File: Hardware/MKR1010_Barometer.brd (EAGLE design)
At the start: 160 x 100 mm, 2 parts

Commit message: schematic capture
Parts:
- added D1: 1N4001, SparkFun-DiscreteSemi:DIODE-1N4001
- added J1: (no value), con-jack:SPC4077
- added J2, J3: 1X2-3.5MM, adafruit:1X2-3.5MM
- added M1: MOTOR10MM, SparkFun-Electromechanical:VIBE-MOTOR-10MM
- added T1: TIP122, transistor:TO220
- R1: value (none) -> 220
- renumbered U$1 to MKR1010
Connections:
- new net GND: D1.A, J1.1, J3.1, T1.3
- new net N$2: R1.1, T1.1
- new net N$3: D1.C, M1.-, T1.2
- new net N$4: J1.3, J2.2, M1.+, MKR1010.P$23
- new net N$5: J2.1, MKR1010.P$7
- net N$1: now also MKR1010.P$6; no longer MKR1010.P$25
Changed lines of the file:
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@@
 <?xml version="1.0" encoding="utf-8"?>
 <!DOCTYPE eagle SYSTEM "eagle.dtd">
-<eagle version="9.2.1">
+<eagle version="9.2.2">
 <drawing>
 <settings>
@@
 <layer number="112" name="tSilk" color="7" fill="1" visible="no" active="yes"/>
 <layer number="113" name="ReferenceLS" color="7" fill="1" visible="no" active="no"/>
+<layer number="114" name="Badge_Outline" color="7" fill="1" visible="yes" active="yes"/>
+<layer number="115" name="ReferenceISLANDS" color="7" fill="1" visible="yes" active="yes"/>
 <layer number="116" name="Patch_BOT" color="9" fill="4" visible="no" active="yes"/>
 <layer number="118" name="Rect_Pads" color="7" fill="1" visible="no" active="no"/>
@@
 </autorouter>
 <elements>
-<element name="U$1" library="adafruit" library_urn="urn:adsk.eagle:library:420" package="ARDUINOMICRO" value="ARDUINOMICRO" x="34.29" y="73.66" smashed="yes"/>
-<element name="R1" library="adafruit" library_urn="urn:adsk.eagle:library:420" package="0207/12" value="" x="36.83" y="53.34" smashed="yes" rot="R90">
+<element name="MKR1010" library="adafruit" library_urn="urn:adsk.eagle:library:420" package="ARDUINOMICRO" value="ARDUINOMICRO" x="34.29" y="73.66" smashed="yes"/>
+<element name="R1" library="adafruit" library_urn="urn:adsk.eagle:library:420" package="0207/12" value="220" x="36.83" y="53.34" smashed="yes" rot="R90">
 <attribute name="NAME" x="35.433" y="50.165" size="1.27" layer="25" ratio="10" rot="R90"/>
 <attribute name="VALUE" x="37.5158" y="51.054" size="1.27" layer="27" ratio="10" rot="R90"/>
+</element>
+<element name="D1" library="SparkFun-DiscreteSemi" library_urn="urn:adsk.eagle:library:514" package="DIODE-1N4001" package3d_urn="urn:adsk.eagle:package:38453/1" value="1N4001" x="6.35" y="-2.54" smashed="yes">
+<attribute name="NAME" x="6.35" y="-1.016" size="0.6096" layer="25" font="vector" ratio="20" align="bottom-center"/>
+<attribute name="PROD_ID" value="DIO-09176" x="6.35" y="-2.54" size="1.778" layer="27" display="off"/>
+<attribute name="VALUE" x="6.35" y="-4.064" size="0.6096" layer="27" font="vector" ratio="20" align="top-center"/>
+</element>
+<element name="T1" library="transistor" library_urn="urn:adsk.eagle:library:402" package="TO220" package3d_urn="urn:adsk.eagle:package:29897/1" value="TIP122" x="-6.35" y="3.81" smashed="yes">
+<attribute name="NAME" x="-10.16" y="9.017" size="1.778" layer="25" ratio="10"/>
+<attribute name="VALUE" x="-10.287" y="6.35" size="1.778" layer="27" ratio="10"/>
+</element>
+<element name="M1" library="SparkFun-Electromechanical" library_urn="urn:adsk.eagle:library:516" package="VIBE-MOTOR-10MM" package3d_urn="urn:adsk.eagle:package:38555/1" value="MOTOR10MM" x="-2.54" y="-10.16" smashed="yes">
+<attribute name="NAME" x="-7.747" y="-10.16" size="0.6096" layer="25" font="vector" ratio="20" rot="R90" align="bottom-center"/>
+<attribute name="PROD_ID" value="COMP-08572" x="-2.54" y="-10.16" size="1.778" layer="27" display="off"/>
+<attribute name="SF_SKU" value="ROB-08449" x="-2.54" y="-10.16" size="1.778" layer="27" display="off"/>
+<attribute name="VALUE" x="-7.239" y="-10.16" size="0.6096" layer="27" font="vector" ratio="20" rot="R90" align="top-center"/>
+</element>
+<element name="J1" library="con-jack" library_urn="urn:adsk.eagle:library:154" package="SPC4077" package3d_urn="urn:adsk.eagle:package:7492/1" value="" x="0" y="-25.4" smashed="yes">
+<attribute name="MF" value="" x="0" y="-25.4" size="1.778" layer="27" display="off"/>
+<attribute name="MPN" value="" x="0" y="-25.4" size="1.778" layer="27" display="off"/>
+<attribute name="NAME" x="-10.16" y="-20.32" size="1.27" layer="25"/>
+<attribute name="OC_FARNELL" value="unknown" x="0" y="-25.4" size="1.778" layer="27" display="off"/>
+<attribute name="OC_NEWARK" value="unknown" x="0" y="-25.4" size="1.778" layer="27" display="off"/>
+<attribute name="VALUE" x="-10.16" y="-31.75" size="1.27" layer="27"/>
+</element>
+<element name="J2" library="adafruit" library_urn="urn:adsk.eagle:library:420" package="1X2-3.5MM" package3d_urn="urn:adsk.eagle:package:6240635/1" value="1X2-3.5MM" x="-16.51" y="-26.67" smashed="yes">
+<attribute name="NAME" x="-13.51" y="-21.67" size="1.27" layer="25" rot="R180"/>
+</element>
+<element name="J3" library="adafruit" library_urn="urn:adsk.eagle:library:420" package="1X2-3.5MM" package3d_urn="urn:adsk.eagle:package:6240635/1" value="1X2-3.5MM" x="-24.13" y="-26.67" smashed="yes">
+<attribute name="NAME" x="-21.13" y="-21.67" size="1.27" layer="25" rot="R180"/>
 </element>
 </elements>
 <signals>
 <signal name="N$1">
-<contactref element="U$1" pad="P$25"/>
+<contactref element="MKR1010" pad="P$6"/>
 <contactref element="R1" pad="2"/>
-<wire x1="36.83" y1="59.69" x2="36.83" y2="66.04" width="0" layer="19" extent="1-1"/>
+<wire x1="36.83" y1="59.69" x2="26.67" y2="81.28" width="0" layer="19" extent="1-1"/>
+</signal>
+<signal name="N$2">
+<contactref element="R1" pad="1"/>
+<contactref element="T1" pad="1"/>
+<wire x1="-8.89" y1="-2.54" x2="36.83" y2="46.99" width="0" layer="19" extent="1-1"/>
+</signal>
+<signal name="N$3">
+<contactref element="M1" pad="-"/>
+<contactref element="T1" pad="2"/>
+<contactref element="D1" pad="C"/>
+<wire x1="-6.35" y1="-2.54" x2="-8.89" y2="-12.7" width="0" layer="19" extent="1-1"/>
+<wire x1="11.43" y1="-2.54" x2="-6.35" y2="-2.54" width="0" layer="19" extent="1-1"/>
+</signal>
+<signal name="GND">
+<contactref element="T1" pad="3"/>
+<contactref element="D1" pad="A"/>
+<contactref element="J3" pad="1"/>
+<contactref element="J1" pad="1"/>
+<wire x1="-3" y1="-25.4" x2="-22.33" y2="-26.67" width="0" layer="19" extent="1-1"/>
+<wire x1="-3.81" y1="-2.54" x2="-3" y2="-25.4" width="0" layer="19" extent="1-1"/>
+<wire x1="1.27" y1="-2.54" x2="-3.81" y2="-2.54" width="0" layer="19" extent="1-1"/>
+</signal>
+<signal name="N$5">
+<contactref element="MKR1010" pad="P$7"/>
+<contactref element="J2" pad="1"/>
+<wire x1="-14.71" y1="-26.67" x2="29.21" y2="81.28" width="0" layer="19" extent="1-1"/>
+</signal>
+<signal name="N$4">
+<contactref element="J1" pad="3"/>
+<contactref element="M1" pad="+"/>
+<contactref element="MKR1010" pad="P$23"/>
+<contactref element="J2" pad="2"/>
+<wire x1="-7.54" y1="-14.06" x2="41.91" y2="66.04" width="0" layer="19" extent="1-1"/>
+<wire x1="3" y1="-25.4" x2="-7.54" y2="-14.06" width="0" layer="19" extent="1-1"/>
+<wire x1="-18.21" y1="-26.67" x2="-7.54" y2="-14.06" width="0" layer="19" extent="1-1"/>
 </signal>
 </signals>
@@
 with this version.
 </note>
+<note version="8.3" severity="warning">
+Since Version 8.3, EAGLE supports URNs for individual library
+assets (packages, symbols, and devices). The URNs of those assets
+will not be understood (or retained) with this version.
+</note>
+<note version="8.3" severity="warning">
+Since Version 8.3, EAGLE supports the association of 3D packages
+with devices in libraries, schematics, and board files. Those 3D
+packages will not be understood (or retained) with this version.
+</note>
 </compatibility>

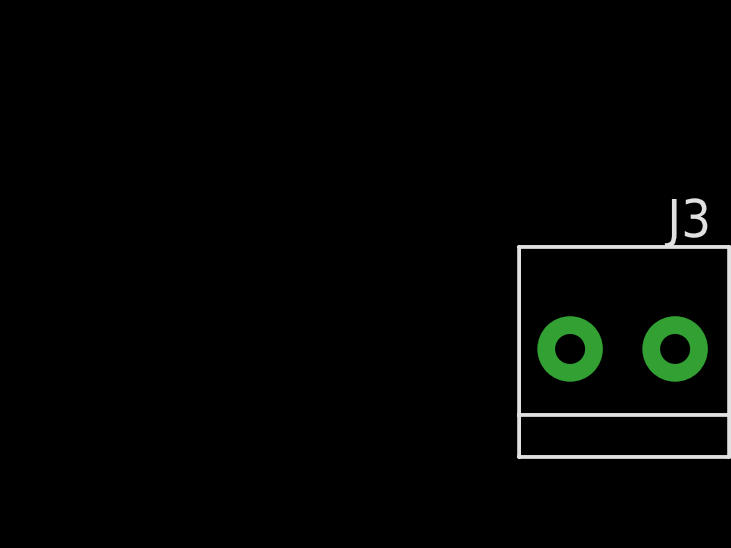
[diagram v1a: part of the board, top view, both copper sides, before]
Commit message: added terminal to attach MPL115A2
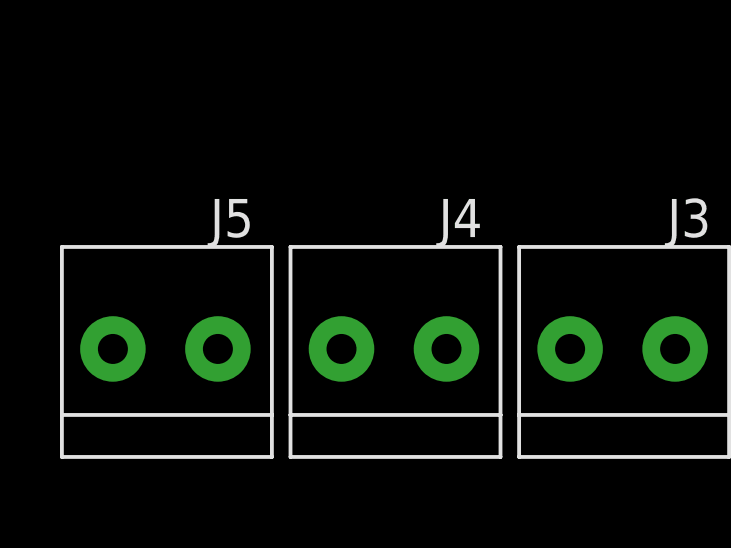
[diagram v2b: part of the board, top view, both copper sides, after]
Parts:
- added J4, J5: 1X2-3.5MM, adafruit:1X2-3.5MM
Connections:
- new net N$6: J4.1, MKR1010.P$18
- new net N$7: J4.2, MKR1010.P$19
- net GND: now also J5.2
- net N$4: now also J5.1
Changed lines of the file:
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@@
 <attribute name="NAME" x="-21.13" y="-21.67" size="1.27" layer="25" rot="R180"/>
+</element>
+<element name="J4" library="adafruit" library_urn="urn:adsk.eagle:library:420" package="1X2-3.5MM" package3d_urn="urn:adsk.eagle:package:6240635/1" value="1X2-3.5MM" x="-31.75" y="-26.67" smashed="yes">
+<attribute name="NAME" x="-28.75" y="-21.67" size="1.27" layer="25" rot="R180"/>
+</element>
+<element name="J5" library="adafruit" library_urn="urn:adsk.eagle:library:420" package="1X2-3.5MM" package3d_urn="urn:adsk.eagle:package:6240635/1" value="1X2-3.5MM" x="-39.37" y="-26.67" smashed="yes">
+<attribute name="NAME" x="-36.37" y="-21.67" size="1.27" layer="25" rot="R180"/>
 </element>
 </elements>
@@
 <contactref element="J3" pad="1"/>
 <contactref element="J1" pad="1"/>
+<contactref element="J5" pad="2"/>
+<wire x1="-22.33" y1="-26.67" x2="-41.07" y2="-26.67" width="0" layer="19" extent="1-1"/>
 <wire x1="-3" y1="-25.4" x2="-22.33" y2="-26.67" width="0" layer="19" extent="1-1"/>
 <wire x1="-3.81" y1="-2.54" x2="-3" y2="-25.4" width="0" layer="19" extent="1-1"/>
@@
 <contactref element="MKR1010" pad="P$23"/>
 <contactref element="J2" pad="2"/>
+<contactref element="J5" pad="1"/>
 <wire x1="-7.54" y1="-14.06" x2="41.91" y2="66.04" width="0" layer="19" extent="1-1"/>
 <wire x1="3" y1="-25.4" x2="-7.54" y2="-14.06" width="0" layer="19" extent="1-1"/>
 <wire x1="-18.21" y1="-26.67" x2="-7.54" y2="-14.06" width="0" layer="19" extent="1-1"/>
+<wire x1="-37.57" y1="-26.67" x2="-18.21" y2="-26.67" width="0" layer="19" extent="1-1"/>
+</signal>
+<signal name="N$6">
+<contactref element="MKR1010" pad="P$18"/>
+<contactref element="J4" pad="1"/>
+<wire x1="-29.95" y1="-26.67" x2="54.61" y2="66.04" width="0" layer="19" extent="1-1"/>
+</signal>
+<signal name="N$7">
+<contactref element="MKR1010" pad="P$19"/>
+<contactref element="J4" pad="2"/>
+<wire x1="-33.45" y1="-26.67" x2="52.07" y2="66.04" width="0" layer="19" extent="1-1"/>
 </signal>
 </signals>
